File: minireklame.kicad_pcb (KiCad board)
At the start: 2 copper layers, 126.7 x 105.9 mm, 64 parts, among them IC1 ATXMEGA64A4U-A, P0 CONN_01X04, P1 CONN_01X04, P10 CONN_01X04, P11 CONN_01X04, P12 CONN_01X04, P13 CONN_01X04, P14 CONN_01X04, P15 CONN_01X04, P17 Phoenix_508_2pos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

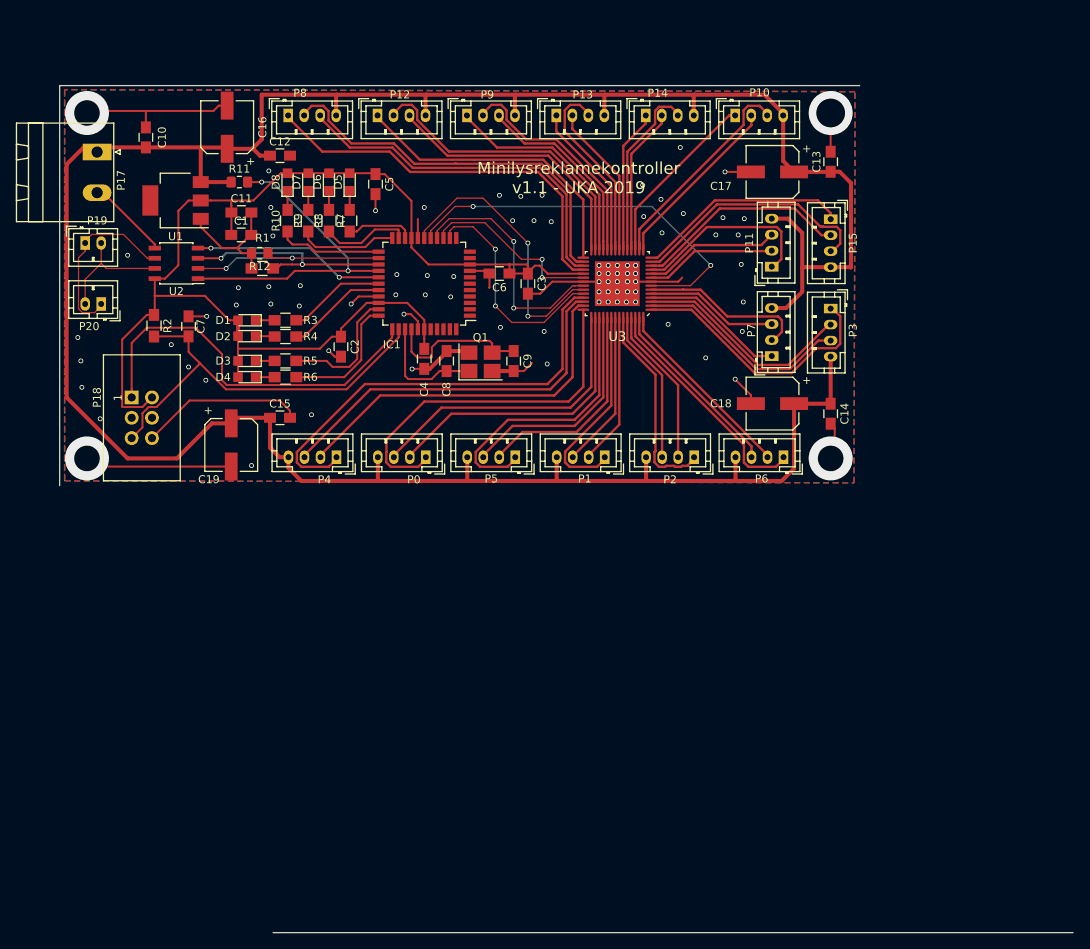
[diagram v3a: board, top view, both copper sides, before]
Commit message: Fixed keepout area
Fixed minor bug in keepout area.
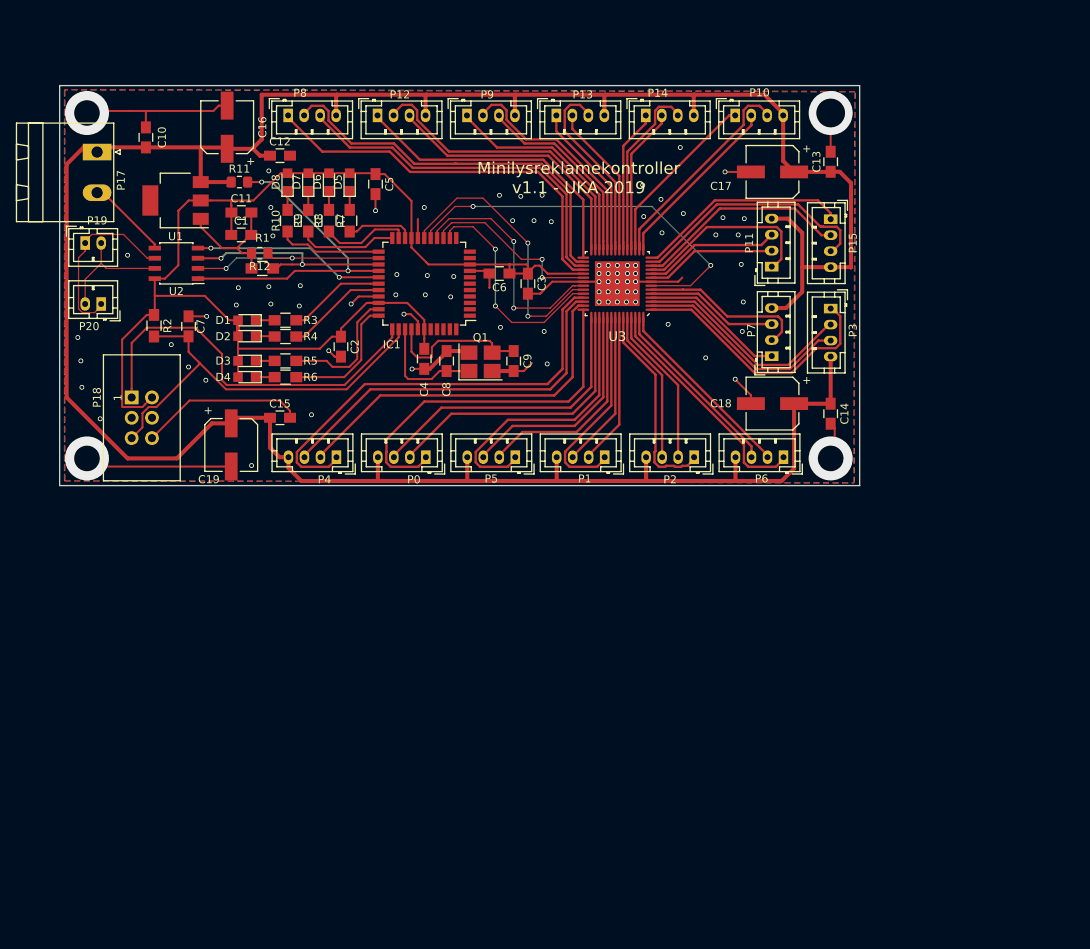
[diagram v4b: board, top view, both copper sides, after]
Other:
- board size 126.7 x 105.9 mm -> 100 x 50 mm
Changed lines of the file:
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@@
   (general
     (thickness 1.6)
-    (drawings 4)
+    (drawings 5)
     (tracks 862)
     (zones 0)
@@
     )
   )
+  (gr_line (start 70 100) (end 170 100) (layer Edge.Cuts) (width 0.15))
+  (gr_line (start 170 50) (end 170 100) (layer Edge.Cuts) (width 0.15))
   (gr_text "Minilysreklamekontroller\nv1.1 - UKA 2019" (at 134.879 61.552) (layer F.SilkS)
     (effects (font (size 1.5 1.5) (thickness 0.3)))
   )
   (gr_line (start 70 50) (end 70 100) (layer Edge.Cuts) (width 0.15))
-  (gr_line (start 196.67 155.88) (end 96.67 155.88) (layer Edge.Cuts) (width 0.15))
   (gr_line (start 70 50) (end 170 50) (layer Edge.Cuts) (width 0.15))
   (segment (start 113.975 69.06) (end 113.975 64.415) (width 0.254) (layer F.Cu) (net 1))
